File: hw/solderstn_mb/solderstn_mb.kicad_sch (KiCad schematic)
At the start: 0 parts

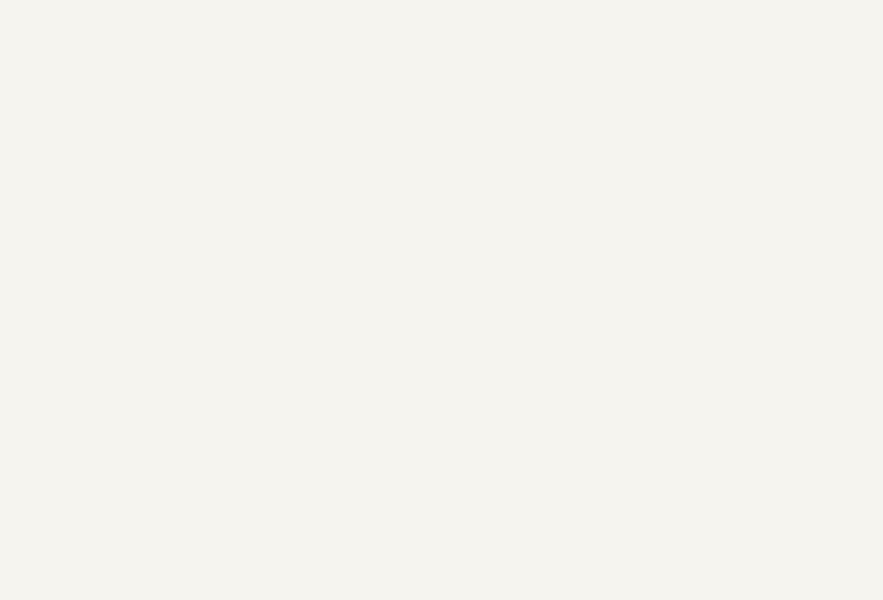
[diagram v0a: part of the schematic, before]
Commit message: Placeholder 3d-models for rear-panel (w. conns), PSU, Bottom-plate, front-panel (w. conns), outer fp
With these placeholder mech. objects, the build-in 3d view of MB pcb features most of the mechanical
objects that constrain components placements. So 3d-view can be used to quickly check and iterate
placements to avoid 3d collisions, without having to first export MB STEP into FreeCAD and muck around
only to have to repeat again for each iteration
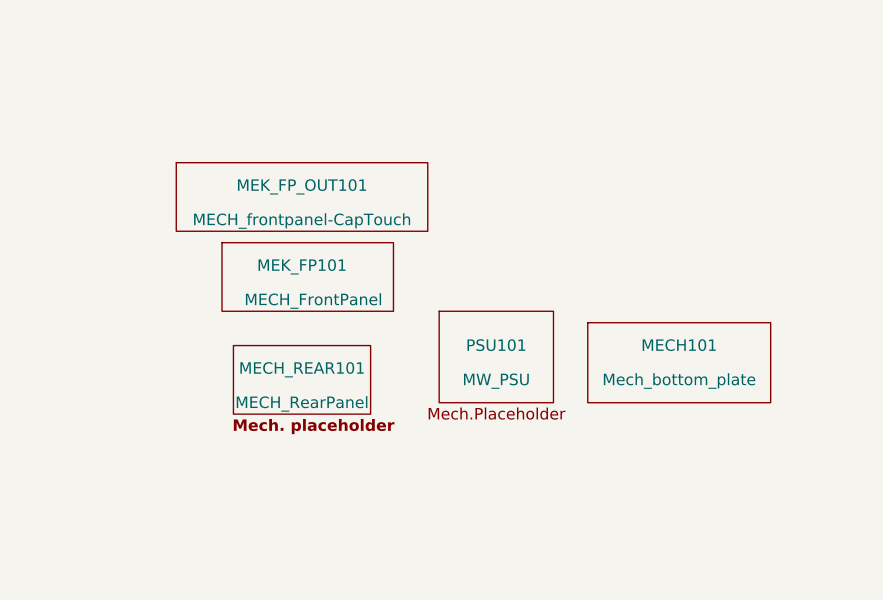
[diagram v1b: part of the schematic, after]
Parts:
- added MECH101: Mech_bottom_plate, customlib_mj_fp:MECH_BTM_PLATE, symbol customlib_mj:Mech_bottom_plate
- added MECH_REAR101: MECH_RearPanel, customlib_mj_fp:Mech_RearPanel, symbol customlib_mj:MECH_RearPanel
- added MEK_FP101: MECH_FrontPanel, customlib_mj_fp:Mech_frontpanel, symbol customlib_mj:MECH_FrontPanel
- added MEK_FP_OUT101: MECH_frontpanel-CapTouch, customlib_mj_fp:Mech_Frontpanel_CapTouch, symbol customlib_mj:MECH_frontpanel-CapTouch
- added PSU101: MW_PSU, customlib_mj_fp:MW_PSU, symbol customlib_mj:MW_PSU
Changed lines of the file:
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@@
     (effects (font (size 1.27 1.27) (thickness 0.254) bold) (justify left bottom))
   )
+  (symbol (lib_id "customlib_mj:MECH_RearPanel") (at 228.6 137.16 0) (unit 1)
+    (in_bom no) (on_board yes)
+    (property "Reference" "MECH_REAR101" (id 0) (at 228.6 135.89 0))
+    (property "Value" "MECH_RearPanel" (id 1) (at 228.6 139.7 0))
+    (property "Footprint" "customlib_mj_fp:Mech_RearPanel" (id 2) (at 228.6 137.16 0)
+      (effects (font (size 1.27 1.27)) hide)
+    )
+    (property "Datasheet" "" (id 3) (at 228.6 137.16 0)
+      (effects (font (size 1.27 1.27)) hide)
+    )
+  )
+  (symbol (lib_id "customlib_mj:MW_PSU") (at 250.19 133.35 0) (unit 1)
+    (in_bom no) (on_board yes)
+    (property "Reference" "PSU101" (id 0) (at 250.19 133.35 0))
+    (property "Value" "MW_PSU" (id 1) (at 250.19 137.16 0))
+    (property "Footprint" "customlib_mj_fp:MW_PSU" (id 2) (at 250.19 133.35 0)
+      (effects (font (size 1.27 1.27)) hide)
+    )
+    (property "Datasheet" "" (id 3) (at 250.19 133.35 0)
+      (effects (font (size 1.27 1.27)) hide)
+    )
+  )
+  (symbol (lib_id "customlib_mj:Mech_bottom_plate") (at 270.51 134.62 0) (unit 1)
+    (in_bom yes) (on_board yes)
+    (property "Reference" "MECH101" (id 0) (at 270.51 133.35 0))
+    (property "Value" "Mech_bottom_plate" (id 1) (at 270.51 137.16 0))
+    (property "Footprint" "customlib_mj_fp:MECH_BTM_PLATE" (id 2) (at 270.51 134.62 0)
+      (effects (font (size 1.27 1.27)) hide)
+    )
+    (property "Datasheet" "" (id 3) (at 270.51 134.62 0)
+      (effects (font (size 1.27 1.27)) hide)
+    )
+  )
+  (symbol (lib_id "customlib_mj:MECH_frontpanel-CapTouch") (at 228.6 116.84 0) (unit 1)
+    (in_bom no) (on_board yes)
+    (property "Reference" "MEK_FP_OUT101" (id 0) (at 228.6 115.57 0))
+    (property "Value" "MECH_frontpanel-CapTouch" (id 1) (at 228.6 119.38 0))
+    (property "Footprint" "customlib_mj_fp:Mech_Frontpanel_CapTouch" (id 2) (at 228.6 116.84 0)
+      (effects (font (size 1.27 1.27)) hide)
+    )
+    (property "Datasheet" "" (id 3) (at 228.6 116.84 0)
+      (effects (font (size 1.27 1.27)) hide)
+    )
+  )
+  (symbol (lib_id "customlib_mj:MECH_FrontPanel") (at 228.6 125.73 0) (unit 1)
+    (in_bom no) (on_board yes)
+    (property "Reference" "MEK_FP101" (id 0) (at 228.6 124.46 0))
+    (property "Value" "MECH_FrontPanel" (id 1) (at 229.87 128.27 0))
+    (property "Footprint" "customlib_mj_fp:Mech_frontpanel" (id 2) (at 228.6 125.73 0)
+      (effects (font (size 1.27 1.27)) hide)
+    )
+    (property "Datasheet" "" (id 3) (at 228.6 125.73 0)
+      (effects (font (size 1.27 1.27)) hide)
+    )
+  )
   (sheet (at 96.52 72.39) (size 35.56 35.56) (fields_autoplaced)
     (stroke (width 0) (type solid) (color 0 0 0 0))
@@
       (reference "#PWR0230") (unit 1) (value "GND") (footprint "")
     )
-    (path "/00000000-0000-0000-0000-00005f472b62/00000000-0000-0000-0000-00005fa83e97"
-      (reference "#PWR0301") (unit 1) (value "GND") (footprint "")
-    )
     (path "/00000000-0000-0000-0000-00005f472b62/00000000-0000-0000-0000-00005fb3ddd8"
       (reference "#PWR0302") (unit 1) (value "+VDC") (footprint "")
@@
       (reference "#PWR0904") (unit 1) (value "GND") (footprint "")
     )
+    (path "/00000000-0000-0000-0000-00005f472fc2/00000000-0000-0000-0000-00006030e740"
+      (reference "#PWR0905") (unit 1) (value "GND") (footprint "")
+    )
+    (path "/00000000-0000-0000-0000-00005f472fc2/00000000-0000-0000-0000-00006032797d"
+      (reference "#PWR0906") (unit 1) (value "GND") (footprint "")
+    )
     (path "/00000000-0000-0000-0000-00005f4730b9/00000000-0000-0000-0000-000060476b76"
       (reference "#PWR01001") (unit 1) (value "GND") (footprint "")
@@
       (reference "#PWR02112") (unit 1) (value "VDD") (footprint "")
     )
-    (path "/00000000-0000-0000-0000-00005eacd927/00000000-0000-0000-0000-00005fb940e3/00000000-0000-0000-0000-00005fbba67b"
-      (reference "#PWR02113") (unit 1) (value "GND") (footprint "")
-    )
     (path "/00000000-0000-0000-0000-00005eacd927/00000000-0000-0000-0000-00005fb940e3/00000000-0000-0000-0000-00005fbb8da6"
       (reference "#PWR02114") (unit 1) (value "VDD") (footprint "")
@@
       (reference "#PWR02217") (unit 1) (value "GND") (footprint "")
     )
-    (path "/00000000-0000-0000-0000-00005f472fc2/00000000-0000-0000-0000-00006030e740"
-      (reference "#PWR?") (unit 1) (value "GND") (footprint "")
-    )
-    (path "/00000000-0000-0000-0000-00005f472fc2/00000000-0000-0000-0000-00006032797d"
-      (reference "#PWR?") (unit 1) (value "GND") (footprint "")
-    )
     (path "/00000000-0000-0000-0000-00005eacd927/00000000-0000-0000-0000-00005ebf9055"
       (reference "#TXT02001") (unit 1) (value "STM32_bootmodes") (footprint "")
     )
-    (path "/00000000-0000-0000-0000-00005eacd927/00000000-0000-0000-0000-00005fb940e3/00000000-0000-0000-0000-00005fbb86e2"
-      (reference "BT2101") (unit 1) (value "CR2032_Backup") (footprint "customlib_mj_fp:CR2032_coincell_holder")
-    )
     (path "/00000000-0000-0000-0000-00005ed59cbf/00000000-0000-0000-0000-00005f1778c2"
       (reference "C201") (unit 1) (value "DNP") (footprint "Capacitor_SMD:C_0402_1005Metric")
@@
       (reference "J201") (unit 1) (value "74980104400") (footprint "customlib_mj_fp:74980104400_WE-RJ45_LAN_trx")
     )
-    (path "/00000000-0000-0000-0000-00005f472b62/00000000-0000-0000-0000-00005faa122c"
-      (reference "J301") (unit 1) (value "Conn_WR-FAST_01x04") (footprint "customlib_mj_fp:WR-FAST_508_4_V")
-    )
     (path "/00000000-0000-0000-0000-00005f472b62/00000000-0000-0000-0000-00005faf4a9d"
       (reference "J302") (unit 1) (value "Molex_MicroFit_30-43045-0421") (footprint "customlib_mj_fp:Molex_Micro-Fit_3.0_43045-0421_2x02-1MP_P3.00mm_Horizontal")
@@
       (reference "J503") (unit 1) (value "JST_S2B-PH-SM4-TB") (footprint "customlib_mj_fp:JST_PH_S2B-PH-SM4-TB_1x02-1MP_P2.00mm_Horizontal")
     )
+    (path "/00000000-0000-0000-0000-00005fe3f0d8/e17ced33-6495-4a76-be4f-a3ba73c29ce8"
+      (reference "J801") (unit 1) (value "alt-placement") (footprint "customlib_mj_fp:SMA_Molex_73251-2200_Horizontal")
+    )
     (path "/00000000-0000-0000-0000-00005f4730b9/00000000-0000-0000-0000-00005fa36c31"
       (reference "J1001") (unit 1) (value "SJ-3571N") (footprint "customlib_mj_fp:SJ-3571N")
@@
       (reference "M601") (unit 1) (value "Fan_4pin") (footprint "Connector:FanPinHeader_1x04_P2.54mm_Vertical")
     )
+    (path "/63b27424-65cf-4576-aae0-9c3aa81dada6"
+      (reference "MECH101") (unit 1) (value "Mech_bottom_plate") (footprint "customlib_mj_fp:MECH_BTM_PLATE")
+    )
+    (path "/4d9ece6b-359f-43bb-9099-2bd2946d206c"
+      (reference "MECH_REAR101") (unit 1) (value "MECH_RearPanel") (footprint "customlib_mj_fp:Mech_RearPanel")
+    )
+    (path "/fba761e9-e0a6-403c-b290-83a8de123db4"
+      (reference "MEK_FP101") (unit 1) (value "MECH_FrontPanel") (footprint "customlib_mj_fp:Mech_frontpanel")
+    )
+    (path "/80bf297f-2fe3-49c0-b509-523d280e1d4e"
+      (reference "MEK_FP_OUT101") (unit 1) (value "MECH_frontpanel-CapTouch") (footprint "customlib_mj_fp:Mech_Frontpanel_CapTouch")
+    )
     (path "/00000000-0000-0000-0000-00005eaeb4b5/00000000-0000-0000-0000-00005f4d1a74"
       (reference "NT401") (unit 1) (value "Net-Tie_2") (footprint "NetTie:NetTie-2_SMD_Pad2.0mm")
     )
+    (path "/5bbd6e4f-9e6b-4482-a2b1-5bac82ea9e34"
+      (reference "PSU101") (unit 1) (value "MW_PSU") (footprint "customlib_mj_fp:MW_PSU")
+    )
     (path "/00000000-0000-0000-0000-00005f472b62/00000000-0000-0000-0000-00005f6ac6c1"
       (reference "Q301") (unit 1) (value "Si4497DY") (footprint "customlib_mj_fp:SOIC-8_3.9x4.9mm_P1.27mm")
@@
       (reference "R603") (unit 1) (value "10k") (footprint "Resistor_SMD:R_0402_1005Metric")
     )
+    (path "/00000000-0000-0000-0000-00005f472fc2/00000000-0000-0000-0000-0000602ecb37"
+      (reference "R901") (unit 1) (value "27k") (footprint "Resistor_SMD:R_0402_1005Metric")
+    )
+    (path "/00000000-0000-0000-0000-00005f472fc2/00000000-0000-0000-0000-00006031fb43"
+      (reference "R902") (unit 1) (value "27k") (footprint "Resistor_SMD:R_0402_1005Metric")
+    )
     (path "/00000000-0000-0000-0000-00005f4730b9/00000000-0000-0000-0000-0000604762d5"
       (reference "R1001") (unit 1) (value "DNM") (footprint "Resistor_SMD:R_0402_1005Metric")
@@
       (reference "R1604") (unit 1) (value "1k") (footprint "Resistor_SMD:R_0402_1005Metric")
     )
+    (path "/00000000-0000-0000-0000-00005eacd927/00000000-0000-0000-0000-00006029eb28"
+      (reference "R1605") (unit 1) (value "10k") (footprint "Resistor_SMD:R_0402_1005Metric")
+    )
     (path "/00000000-0000-0000-0000-00005f785d6e/00000000-0000-0000-0000-00005f788a8e/00000000-0000-0000-0000-00005f5a8042/00000000-0000-0000-0000-00005f5b486d"
       (reference "R1701") (unit 1) (value "15k") (footprint "Resistor_SMD:R_0402_1005Metric")
@@
       (reference "R2203") (unit 1) (value "1k") (footprint "Resistor_SMD:R_0402_1005Metric")
     )
-    (path "/00000000-0000-0000-0000-00005eacd927/00000000-0000-0000-0000-00006029eb28"
-      (reference "R?") (unit 1) (value "10k") (footprint "Resistor_SMD:R_0402_1005Metric")
-    )
-    (path "/00000000-0000-0000-0000-00005f472fc2/00000000-0000-0000-0000-0000602ecb37"
-      (reference "R?") (unit 1) (value "27k") (footprint "Resistor_SMD:R_0402_1005Metric")
-    )
-    (path "/00000000-0000-0000-0000-00005f472fc2/00000000-0000-0000-0000-00006031fb43"
-      (reference "R?") (unit 1) (value "27k") (footprint "Resistor_SMD:R_0402_1005Metric")
-    )
     (path "/00000000-0000-0000-0000-00005eacd927/00000000-0000-0000-0000-00005fb940e3/00000000-0000-0000-0000-00005ff29fef"
